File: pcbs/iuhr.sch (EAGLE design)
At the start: 83 parts, among them Q1 20.000MHz, Q2 MOSFET-NCHANNELSMD

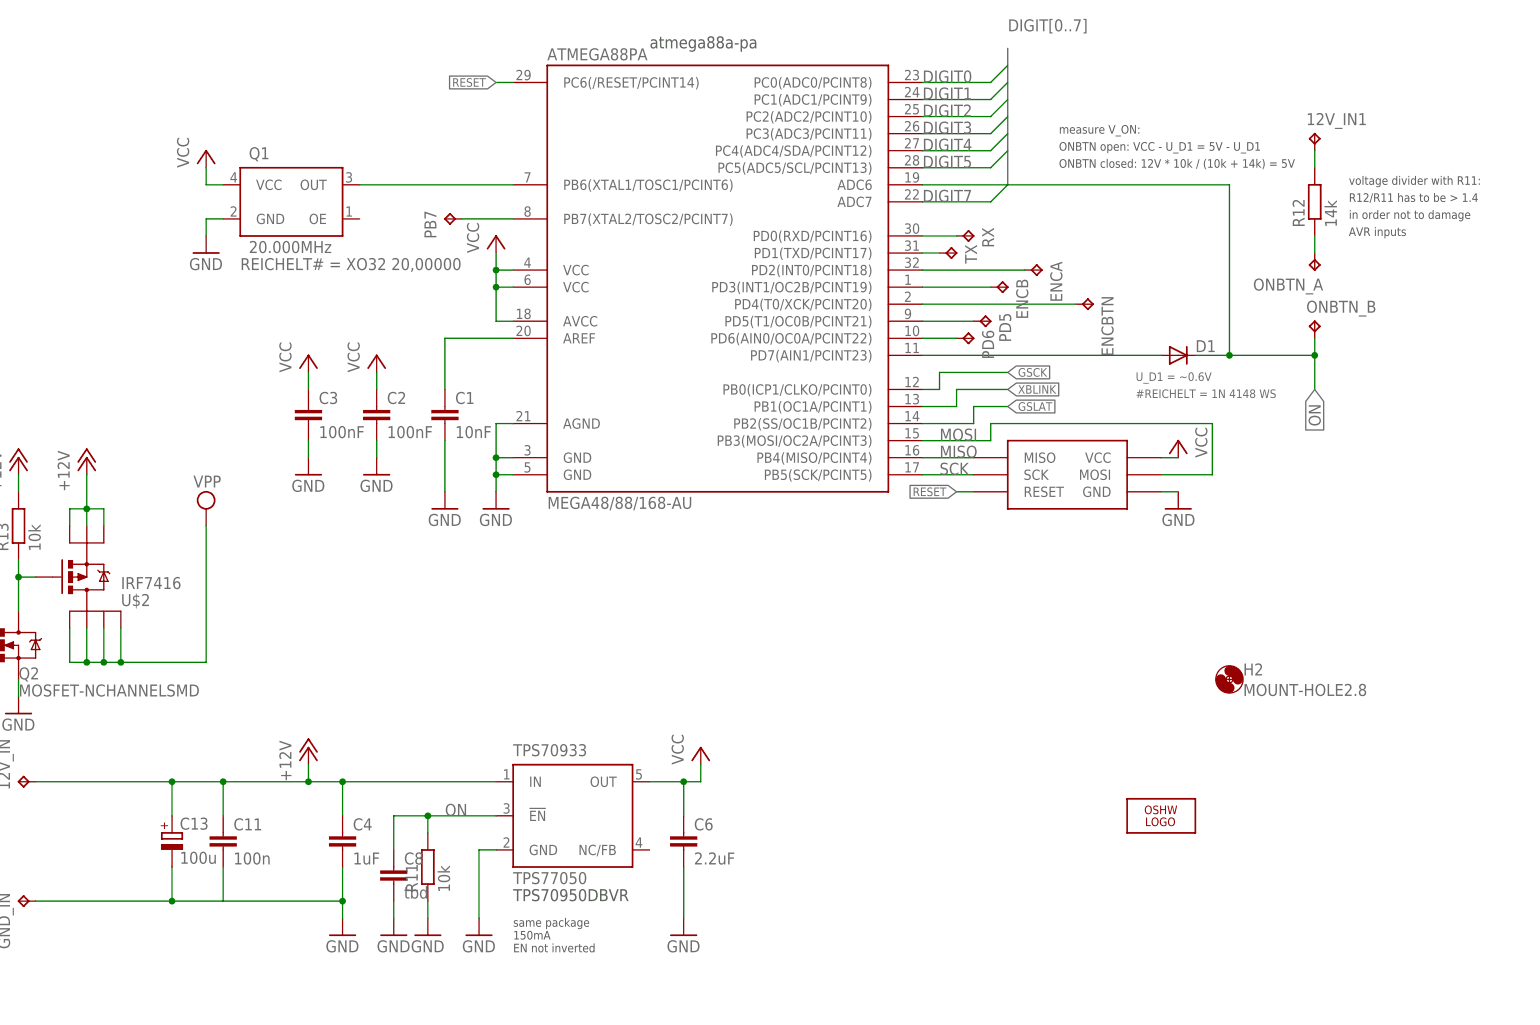
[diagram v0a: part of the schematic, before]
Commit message: Can now use "ON" Switch to turn board off
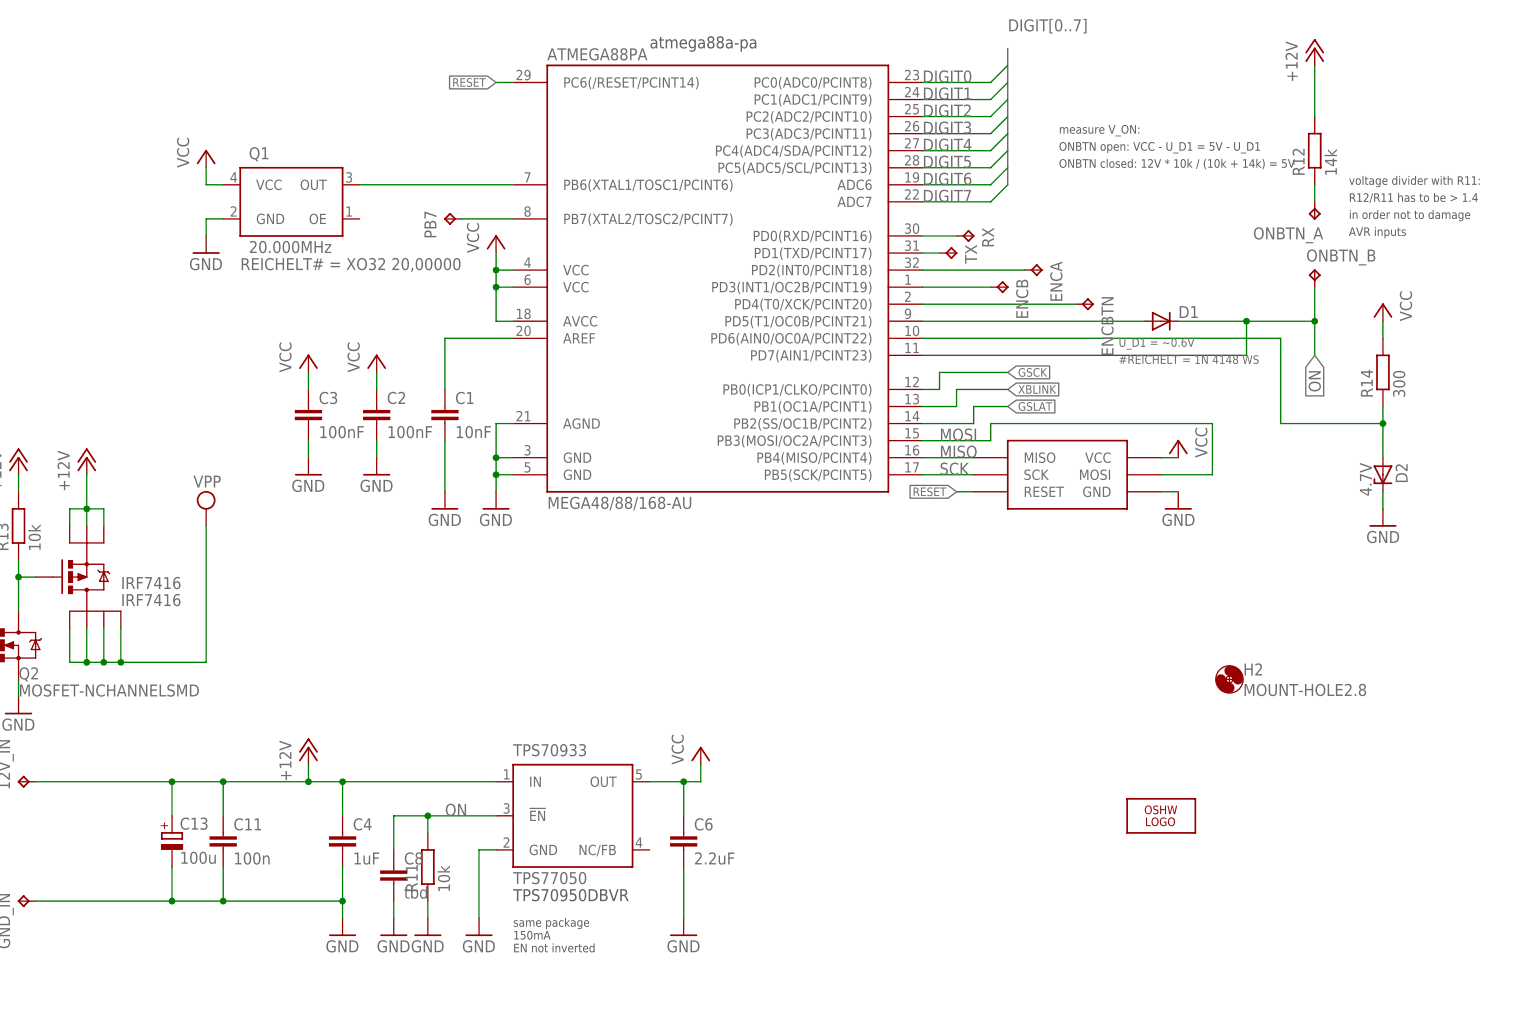
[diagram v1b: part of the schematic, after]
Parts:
- removed 12V_IN1: TPTP20SQ, testpad:TPTP20SQ
- removed PD5, PD6: TPTP15SQ, testpad:TPTP15SQ
- added D2: 4.7V, diode:ZENER-DIODESOT23
- added R14: 300, resistor:R-EU_R0603
- renumbered U$2 to IRF7416
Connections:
- removed net N$63: 12V_IN1.TP, R12.2
- removed net N$64: ATMEGA88PA.PD7(AIN1/PCINT23), D1.A
- net +12V: now also R12.2
- net DIGIT6: now also ATMEGA88PA.ADC6
- net GND: now also D2.C
- net N$56: now also D1.A; no longer PD5.TP
- net N$57: now also D2.A, R14.1; no longer PD6.TP
- net ON: now also ATMEGA88PA.PD7(AIN1/PCINT23); no longer ATMEGA88PA.ADC6
- net VCC: now also R14.2
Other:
- moved on the sheet: D1, ONBTN_A, ONBTN_B, R12

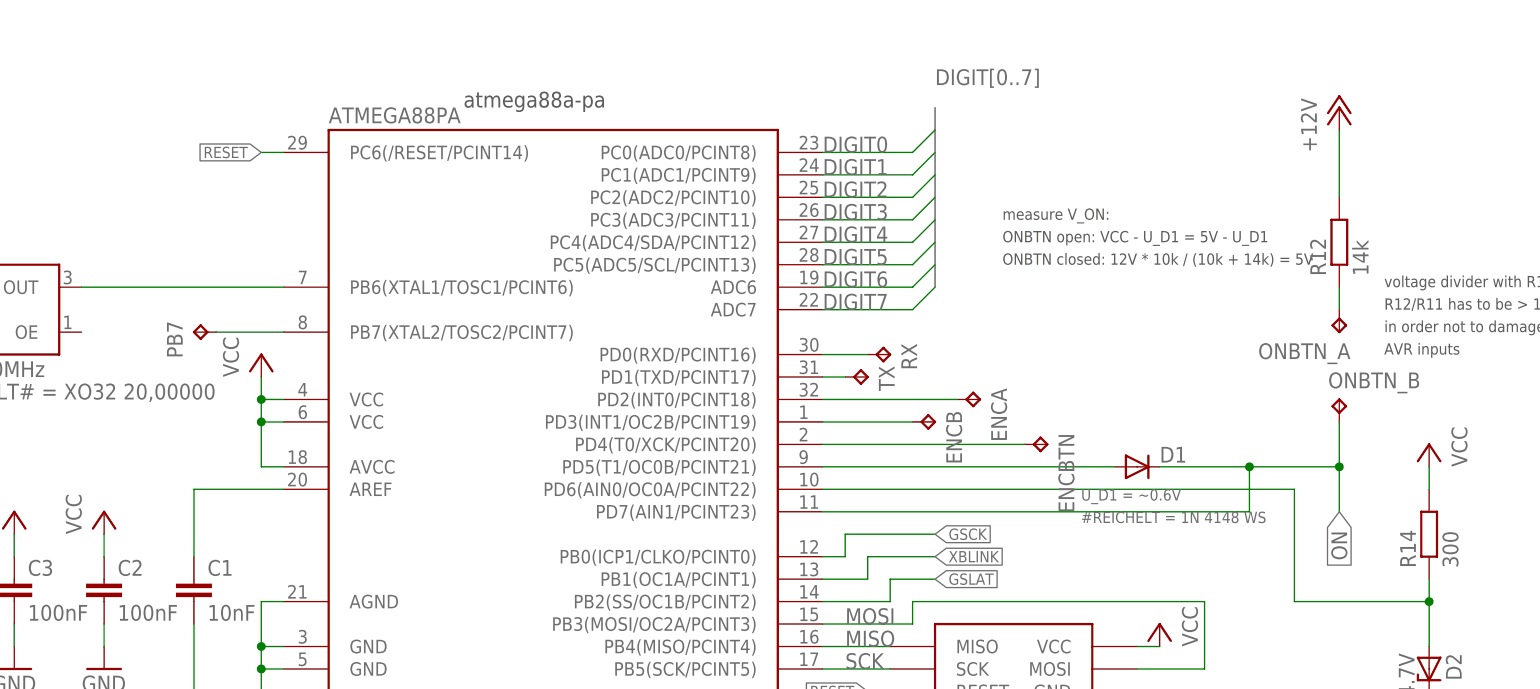
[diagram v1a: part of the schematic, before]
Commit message: Swap functionality of PB7 and PD5
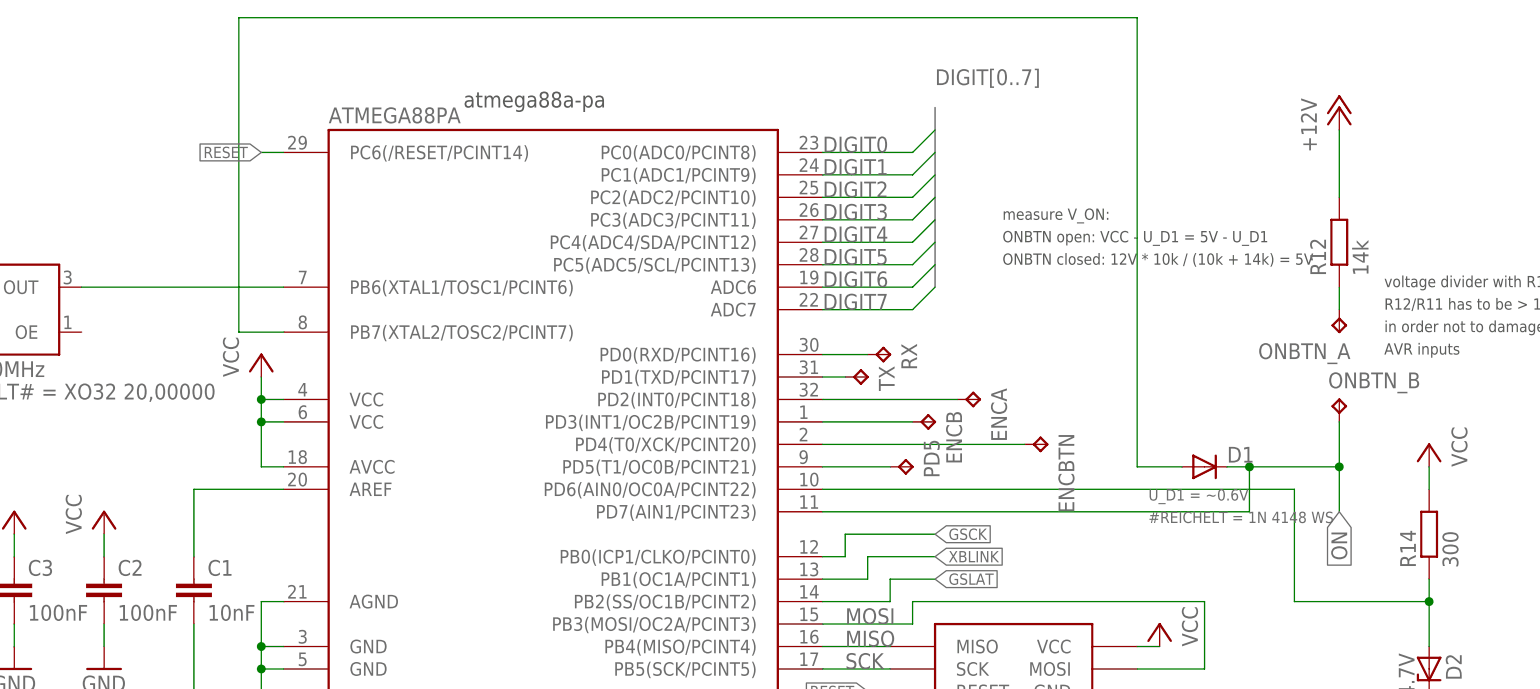
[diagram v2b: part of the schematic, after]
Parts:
- removed PB7: TPTP15SQ, testpad:TPTP15SQ
- added PD5: TPTP15SQ, testpad:TPTP15SQ
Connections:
- net N$56: now also PD5.TP; no longer D1.A
- net N$58: now also D1.A; no longer PB7.TP
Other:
- moved on the sheet: D1
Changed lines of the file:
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@@
 <part name="GND16" library="supply1" deviceset="GND" device=""/>
 <part name="LOGO1" library="ea" deviceset="OSHW_LOGO_8MIL" device="X0200-NT"/>
-<part name="PB7" library="testpad" deviceset="TP" device="TP15SQ"/>
+<part name="PD5" library="testpad" deviceset="TP" device="TP15SQ"/>
 <part name="C7" library="resistor" deviceset="C-EU" device="C0603" value="100nF"/>
 <part name="GND17" library="supply1" deviceset="GND" device=""/>
@@
 <instance part="GND16" gate="1" x="68.58" y="-116.84"/>
 <instance part="LOGO1" gate="G$1" x="208.28" y="43.18"/>
-<instance part="PB7" gate="G$1" x="101.6" y="132.08" rot="MR270"/>
+<instance part="PD5" gate="G$1" x="182.88" y="116.84" rot="MR90"/>
 <instance part="C7" gate="G$1" x="177.8" y="-30.48"/>
 <instance part="GND17" gate="1" x="177.8" y="-40.64"/>
@@
 <attribute name="VALUE" x="38.1" y="60.96" size="1.778" layer="96"/>
 </instance>
-<instance part="D1" gate="G$1" x="208.28" y="116.84">
-<attribute name="IDENTIFIER" x="208.28" y="116.84" size="1.778" layer="96" display="off"/>
-<attribute name="#REICHELT" x="201.93" y="110.49" size="1.27" layer="96" display="both"/>
-<attribute name="U_D1" x="201.93" y="113.03" size="1.27" layer="96" display="both"/>
+<instance part="D1" gate="G$1" x="215.9" y="116.84">
+<attribute name="IDENTIFIER" x="215.9" y="116.84" size="1.778" layer="96" display="off"/>
+<attribute name="#REICHELT" x="209.55" y="110.49" size="1.27" layer="96" display="both"/>
+<attribute name="U_D1" x="209.55" y="113.03" size="1.27" layer="96" display="both"/>
 </instance>
 <instance part="R12" gate="G$1" x="231.14" y="142.24" rot="R90"/>
@@
 <wire x1="231.14" y1="116.84" x2="231.14" y2="111.76" width="0.1524" layer="91"/>
 <junction x="231.14" y="116.84"/>
-<wire x1="210.82" y1="116.84" x2="220.98" y2="116.84" width="0.1524" layer="91"/>
+<wire x1="218.44" y1="116.84" x2="220.98" y2="116.84" width="0.1524" layer="91"/>
 <wire x1="220.98" y1="116.84" x2="231.14" y2="116.84" width="0.1524" layer="91"/>
 <junction x="220.98" y="116.84"/>
@@
 <segment>
 <pinref part="ATMEGA88PA" gate="1" pin="PB7(XTAL2/TOSC2/PCINT7)"/>
-<pinref part="PB7" gate="G$1" pin="TP"/>
-<wire x1="104.14" y1="132.08" x2="111.76" y2="132.08" width="0.1524" layer="91"/>
+<pinref part="D1" gate="G$1" pin="A"/>
+<wire x1="106.68" y1="132.08" x2="111.76" y2="132.08" width="0.1524" layer="91"/>
+<wire x1="213.36" y1="116.84" x2="208.28" y2="116.84" width="0.1524" layer="91"/>
+<wire x1="208.28" y1="116.84" x2="208.28" y2="167.64" width="0.1524" layer="91"/>
+<wire x1="208.28" y1="167.64" x2="106.68" y2="167.64" width="0.1524" layer="91"/>
+<wire x1="106.68" y1="167.64" x2="106.68" y2="132.08" width="0.1524" layer="91"/>
 </segment>
 </net>
@@
 </segment>
 </net>
-<net name="N$56" class="0">
-<segment>
-<pinref part="ATMEGA88PA" gate="1" pin="PD5(T1/OC0B/PCINT21)"/>
-<wire x1="172.72" y1="116.84" x2="205.74" y2="116.84" width="0.1524" layer="91"/>
-<pinref part="D1" gate="G$1" pin="A"/>
-</segment>
-</net>
 <net name="N$57" class="0">
 <segment>
@@
 </segment>
 </net>
+<net name="N$56" class="0">
+<segment>
+<pinref part="ATMEGA88PA" gate="1" pin="PD5(T1/OC0B/PCINT21)"/>
+<pinref part="PD5" gate="G$1" pin="TP"/>
+<wire x1="180.34" y1="116.84" x2="172.72" y2="116.84" width="0.1524" layer="91"/>
+</segment>
+</net>

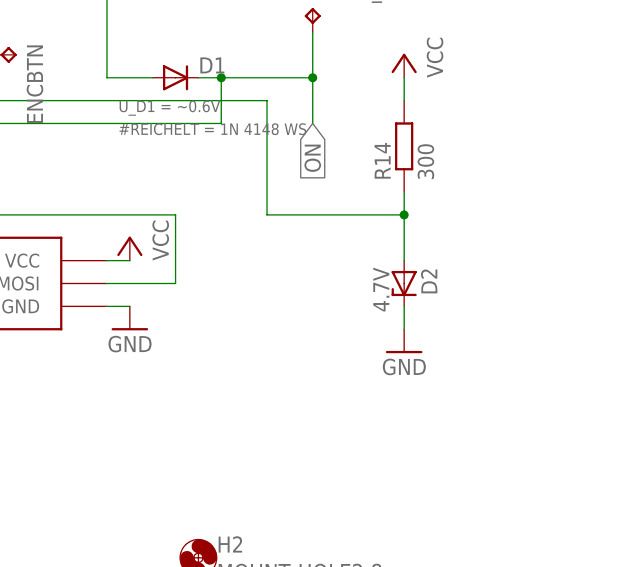
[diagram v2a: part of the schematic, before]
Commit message: Improved GND connectivity
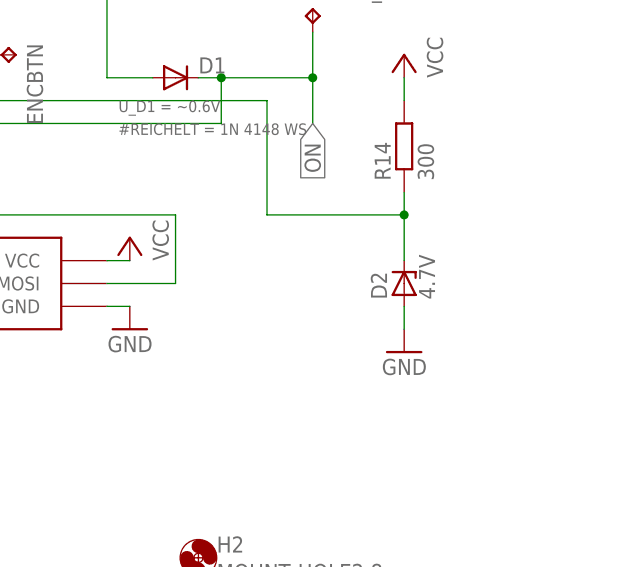
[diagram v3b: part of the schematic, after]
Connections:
- net GND: now also D2.A; no longer D2.C
- net N$57: now also D2.C; no longer D2.A
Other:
- moved on the sheet: D2

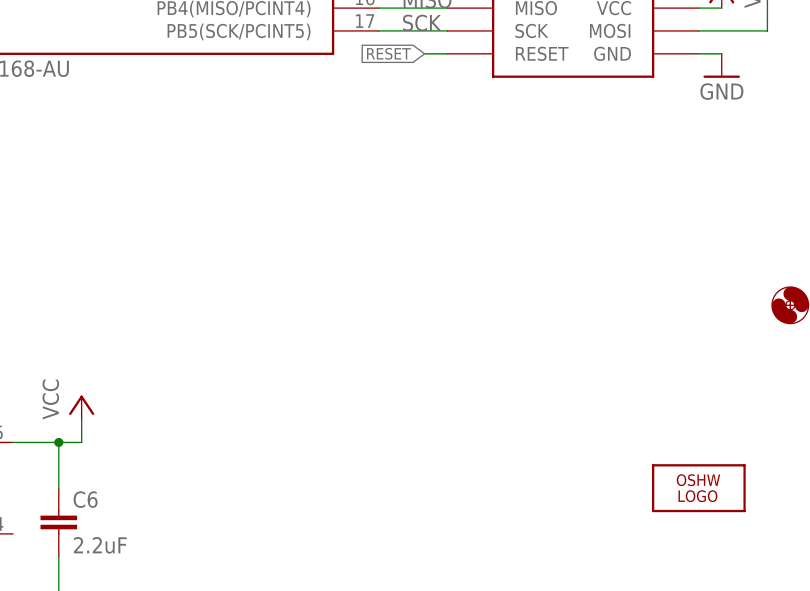
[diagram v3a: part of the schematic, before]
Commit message: Add GND and +5V breakout pads.
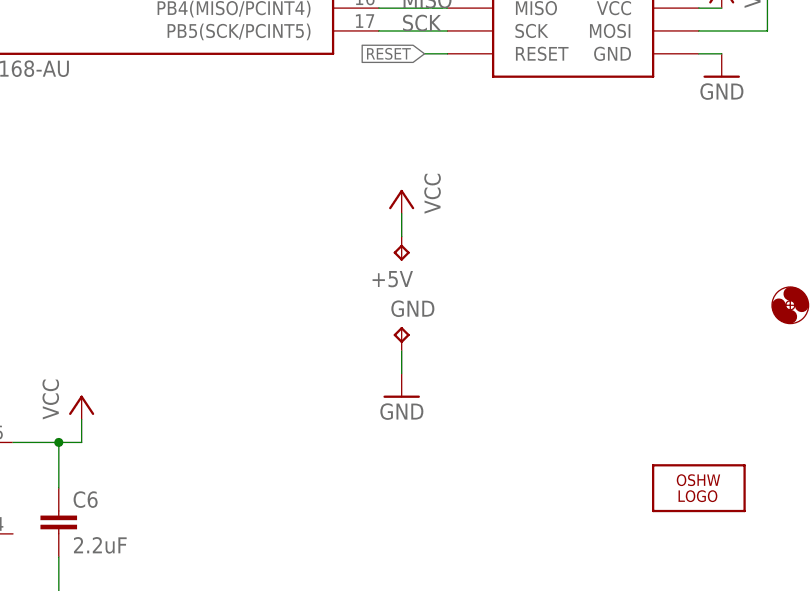
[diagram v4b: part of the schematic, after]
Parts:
- added +5V, GND: TPTP15SQ, testpad:TPTP15SQ
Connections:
- net GND: now also GND.TP
- net VCC: now also +5V.TP
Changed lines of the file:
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@@
 <part name="R7" library="resistor" deviceset="R-EU_" device="R0603" value="33"/>
 <part name="R8" library="resistor" deviceset="R-EU_" device="R0603" value="33"/>
+<part name="P+7" library="supply1" deviceset="VCC" device=""/>
+<part name="GND21" library="supply1" deviceset="GND" device=""/>
+<part name="+5V" library="testpad" deviceset="TP" device="TP15SQ"/>
+<part name="GND" library="testpad" deviceset="TP" device="TP15SQ"/>
 </parts>
 <sheets>
@@
 <instance part="R7" gate="G$1" x="215.9" y="-127"/>
 <instance part="R8" gate="G$1" x="215.9" y="-144.78"/>
+<instance part="P+7" gate="VCC" x="175.26" y="76.2" rot="MR0"/>
+<instance part="GND21" gate="1" x="175.26" y="53.34" rot="MR0"/>
+<instance part="+5V" gate="G$1" x="175.26" y="68.58" rot="R180"/>
+<instance part="GND" gate="G$1" x="175.26" y="60.96"/>
 </instances>
 <busses>
@@
 <wire x1="241.3" y1="91.44" x2="241.3" y2="88.9" width="0.1524" layer="91"/>
 </segment>
+<segment>
+<pinref part="GND21" gate="1" pin="GND"/>
+<pinref part="GND" gate="G$1" pin="TP"/>
+<wire x1="175.26" y1="55.88" x2="175.26" y2="58.42" width="0.1524" layer="91"/>
+</segment>
 </net>
 <net name="VCC" class="0">
@@
 <pinref part="P+6" gate="VCC" pin="VCC"/>
 </segment>
+<segment>
+<pinref part="P+7" gate="VCC" pin="VCC"/>
+<pinref part="+5V" gate="G$1" pin="TP"/>
+<wire x1="175.26" y1="71.12" x2="175.26" y2="73.66" width="0.1524" layer="91"/>
+</segment>
 </net>
